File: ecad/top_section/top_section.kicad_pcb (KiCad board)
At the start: 4 copper layers, 100 x 88 mm, 142 parts, among them J1 JST PH, J2 JST PH, J3 JST SH, J4 JST SH, Q1 RE1C002UN, Q10 RE1C002UN, Q2 RE1C002UN, Q3 RE1C002UN, Q4 RE1C002UN, Q5 RE1C002UN, Q6 RE1C002UN, Q7 RE1C002UN, Q8 RE1C002UN, Q9 RE1C002UN, SW1 PEL12T, SW10 PEL12T, SW11 PEL12T, SW12 PEL12T, SW13 PEL12T, SW14 PEL12T, SW15 PEL12T, SW16 SW_Push, SW17 SW_Push, SW18 SW_Push, SW19 SW_Push, SW2 SW_Push, SW20 SW_Push, SW3 PEL12T, SW4 SW_Push, SW5 PEL12T, SW6 SW_Push, SW7 SW_Push, SW8 PEL12T, SW9 SW_Push, U11 ATtiny1617-M, U12 WS2811, U13 WS2811, U14 WS2811, U15 WS2811, U16 WS2811, U17 WS2811, U18 WS2811, U19 WS2811, U20 WS2811, U21 WS2811

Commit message: [WIP] Layouting a matric led driver
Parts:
- removed the C1 at (61.7, 60.8)
- removed C10, C11, C12, C13, C14, C15, C16, C17, C18, C19, C20, C4, C5, C6, C7, C8, C9: 100n, Capacitor_SMD:C_0603_1608Metric
- removed C22: 10u, Capacitor_SMD:C_0603_1608Metric
- removed Q1, Q10, Q2, Q3, Q4, Q5, Q6, Q7, Q8, Q9: RE1C002UN, Package_TO_SOT_SMD:SOT-416
- removed R1, R11, R13, R15, R17, R19, R21, R22, R23, R24, R25, R26, R3, R32, R33, R34, R35, R5, R7, R9: 68, Resistor_SMD:R_0603_1608Metric
- removed R10, R12, R14, R16, R18, R2, R20, R4, R6, R8: 11k, Resistor_SMD:R_0603_1608Metric
- removed R27, R29: 33, Resistor_SMD:R_0603_1608Metric
- removed U12, U13, U14, U15, U16, U17, U18, U19, U20, U21: WS2811, Package_SO:SOIC-8_3.9x4.9mm_P1.27mm
- added U2: LP5864, woodpecker:Texas_LP586X_VQFN-32-1EP_4x4mm_P0.4mm_EP2.8x2.8mm_ThermalVias, B.Cu at (107.0, 133.9)
- C2, C3: value 100n -> 1u; moved to F.Cu
- D10: value IN-PI32TAR -> 1N4148W; footprint woodpecker:LED_Inolux_IN-PI32TAR_PLCC4_3.2x2.8mm_P1.5mm -> Diode_SMD:D_SOD-123
- D11, D9: value 1N4148W -> LED_BGRA; footprint Diode_SMD:D_SOD-123 -> woodpecker:LED_Inolux_IN-PI32TRRRGB_PLCC4_3.2x2.8mm_P1.5mm
- D12, D16, D18, D20: value BAS16TW -> 1N4148W; footprint Package_TO_SOT_SMD:SOT-363_SC-70-6 -> Diode_SMD:D_SOD-123
- D13, D2, D21, D23, D25: value IN-PI32TAR -> LED_BGRA; footprint woodpecker:LED_Inolux_IN-PI32TAR_PLCC4_3.2x2.8mm_P1.5mm -> woodpecker:LED_Inolux_IN-PI32TRRRGB_PLCC4_3.2x2.8mm_P1.5mm
- D15, D17, D19: value BAS16TW -> LED_BGRA; footprint Package_TO_SOT_SMD:SOT-363_SC-70-6 -> woodpecker:LED_Inolux_IN-PI32TRRRGB_PLCC4_3.2x2.8mm_P1.5mm
- D27, D29, D5, D8: value IN-PI32TAR -> BAS16TW; footprint woodpecker:LED_Inolux_IN-PI32TAR_PLCC4_3.2x2.8mm_P1.5mm -> Package_TO_SOT_SMD:SOT-363_SC-70-6
- D28, D30, D6: value 1N4148W -> BAS16TW; footprint Diode_SMD:D_SOD-123 -> Package_TO_SOT_SMD:SOT-363_SC-70-6
- SW10, SW11, SW12, SW13, SW14, SW15, SW8: value PEL12T -> SW_Push; footprint woodpecker:PEL12T-4xxxS-S1024 -> woodpecker:SW_Hotswap_Kailh_MX_1.00u
- SW17, SW18, SW19, SW20, SW4, SW6, SW7: value SW_Push -> PEL12T; footprint woodpecker:SW_Hotswap_Kailh_MX_1.00u -> woodpecker:PEL12T-4xxxS-S1024
- moved C2 100.4 mm to (100.9, -7.45), turned to 0 degrees
- moved D16 86.7 mm to (142.2, 73.6)
- moved SW11 78.3 mm to (138.0, 82.0), turned to 0 degrees
- moved SW16 76.0 mm to (138.0, 120.0)
- moved C3 68.8 mm to (100.9, -4.93)
- moved SW7 60.1 mm to (62.0, 101.0), turned to -90 degrees
- moved D20 51.8 mm to (85.2, 111.6)
- moved D27 49.6 mm to (76.8, 99.5), turned to 90 degrees
- moved D19 46.2 mm to (81.0, 125.8), turned to 180 degrees
- moved D8 43.9 mm to (57.8, 99.5), turned to 90 degrees
- moved SW6 42.5 mm to (138.0, 63.0), turned to -90 degrees
- moved SW8 42.5 mm to (81.0, 82.0), turned to 0 degrees
- moved J1 41.4 mm to (141.4, 175.3)
- moved J3 40.0 mm to (122.4, 174.0)
- moved D7 38.0 mm to (133.8, 61.5), turned to 90 degrees
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- renumbered C21 to C1, J4 to J2, J2 to J3, J3 to J4, U11 to U1
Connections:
- C2 pad 1: +5V -> +3V3
- C3 pad 1: /RotaryEncoder_COL2/+5V_smooth -> +5V
- D1 pad 1: /COL1 -> (no net)
- D1 pad 6: /RotaryEncoder_COL1/Q_HS -> (no net)
- D10 pad 1: +5V -> /R2_SW
- D10 pad 2: /KeyboardKey_COL4/DOUT -> /KeyboardKey_COL2/SW_ND
- D11 pad 1: /R2_SW -> /C3_LEDB
- D11 pad 2: /KeyboardKey_COL4/SW_ND -> /C3_LEDG
- D12 pad 1: /COL4 -> /R2_SW
- D12 pad 2: /RotaryEncoder_COL4/H_QB -> /KeyboardKey_COL3/SW_ND
- D13 pad 1: +5V -> /C4_LEDB
- D13 pad 2: /KeyboardKey_COL5/DOUT -> /C4_LEDG
- D13 pad 3: GND -> /C4_LEDR
- D13 pad 4: /KeyboardKey_COL4/DOUT -> /R2_LEDA
- D14 pad 2: /KeyboardKey_COL5/SW_ND -> /KeyboardKey_COL4/SW_ND
- D15 pad 1: /COL5 -> /C5_LEDB
- D15 pad 2: /RotaryEncoder_COL5/H_QB -> /C5_LEDG
- D15 pad 3: /RotaryEncoder_COL5/H_QA -> /C5_LEDR
- D15 pad 4: /R1_QA -> /R2_LEDA
- D16 pad 1: /COL1 -> /R2_SW
- D16 pad 2: /RotaryEncoder_COL6/H_QB -> /KeyboardKey_COL5/SW_ND
- D17 pad 1: /COL2 -> /C1_LEDB
- D17 pad 2: /RotaryEncoder_COL7/H_QB -> /C1_LEDG
- D17 pad 3: /RotaryEncoder_COL7/H_QA -> /C1_LEDR
- D17 pad 4: /R3_QA -> /R4_LEDA
- D18 pad 1: /COL3 -> /R4_SW
- D18 pad 2: /RotaryEncoder_COL8/H_QB -> /KeyboardKey_COL6/SW_ND
- D19 pad 1: /COL4 -> /C2_LEDB
- D19 pad 2: /RotaryEncoder_COL9/H_QB -> /C2_LEDG
- D19 pad 3: /RotaryEncoder_COL9/H_QA -> /C2_LEDR
- D19 pad 4: /R3_QA -> /R4_LEDA
- D2 pad 1: +5V -> /C1_LEDB
- D2 pad 2: /KeyboardKey_COL1/DOUT -> /C1_LEDG
- D2 pad 3: GND -> /C1_LEDR
- D2 pad 4: /KeyboardKey_COL1/DIN -> /R2_LEDA
- D20 pad 1: /COL5 -> /R4_SW
- D20 pad 2: /RotaryEncoder_COL10/H_QB -> /KeyboardKey_COL7/SW_ND
- D21 pad 1: +5V -> /C3_LEDB
- D21 pad 2: /KeyboardKey_COL6/DOUT -> /C3_LEDG
- D21 pad 3: GND -> /C3_LEDR
- D21 pad 4: /KeyboardKey_COL6/DIN -> /R4_LEDA
- D22 pad 2: /KeyboardKey_COL6/SW_ND -> /KeyboardKey_COL8/SW_ND
- D23 pad 1: +5V -> /C4_LEDB
- D23 pad 2: /KeyboardKey_COL7/DOUT -> /C4_LEDG
- D23 pad 3: GND -> /C4_LEDR
- D23 pad 4: /KeyboardKey_COL6/DOUT -> /R4_LEDA
- D24 pad 2: /KeyboardKey_COL7/SW_ND -> /KeyboardKey_COL9/SW_ND
- D25 pad 1: +5V -> /C5_LEDB
- D25 pad 2: /KeyboardKey_COL8/DOUT -> /C5_LEDG
- D25 pad 3: GND -> /C5_LEDR
- D25 pad 4: /KeyboardKey_COL7/DOUT -> /R4_LEDA
- D26 pad 2: /KeyboardKey_COL8/SW_ND -> /KeyboardKey_COL10/SW_ND
- D27 pad 1: +5V -> (no net)
- D27 pad 2: /KeyboardKey_COL10/DIN -> /RotaryEncoder_COL7/H_QB
- D27 pad 3: GND -> /RotaryEncoder_COL7/H_QA
- D27 pad 4: /KeyboardKey_COL8/DOUT -> /R3_QA
- D28 pad 1: /R4_SW -> (no net)
- D28 pad 2: /KeyboardKey_COL9/SW_ND -> /RotaryEncoder_COL8/H_QB
- D29 pad 1: +5V -> (no net)
- D29 pad 2: /KeyboardKey_COL10/DOUT -> /RotaryEncoder_COL9/H_QB
- D29 pad 3: GND -> /RotaryEncoder_COL9/H_QA
- D29 pad 4: /KeyboardKey_COL10/DIN -> /R3_QA
- D30 pad 1: /R4_SW -> (no net)
- D30 pad 2: /KeyboardKey_COL10/SW_ND -> /RotaryEncoder_COL10/H_QB
- D4 pad 1: /COL2 -> (no net)
- D4 pad 6: /RotaryEncoder_COL2/Q_HS -> (no net)
- D5 pad 1: +5V -> (no net)
- D5 pad 2: /KeyboardKey_COL2/DOUT -> /RotaryEncoder_COL3/H_QB
- D5 pad 3: GND -> /RotaryEncoder_COL3/H_QA
- D5 pad 4: /KeyboardKey_COL1/DOUT -> /R1_QA
- D6 pad 1: /R2_SW -> (no net)
- D6 pad 2: /KeyboardKey_COL2/SW_ND -> /RotaryEncoder_COL4/H_QB
- D7 pad 1: /COL3 -> (no net)
- D7 pad 2: /RotaryEncoder_COL3/H_QB -> /RotaryEncoder_COL5/H_QB
- D7 pad 3: /RotaryEncoder_COL3/H_QA -> /RotaryEncoder_COL5/H_QA
- D7 pad 6: /RotaryEncoder_COL3/Q_HS -> (no net)
- D8 pad 1: +5V -> (no net)
- D8 pad 2: /KeyboardKey_COL3/DOUT -> /RotaryEncoder_COL6/H_QB
- D8 pad 3: GND -> /RotaryEncoder_COL6/H_QA
- D8 pad 4: /KeyboardKey_COL2/DOUT -> /R3_QA
- D9 pad 1: /R2_SW -> /C2_LEDB
- D9 pad 2: /KeyboardKey_COL3/SW_ND -> /C2_LEDG
- SW1 pad 1: /RotaryEncoder_COL1/OUTR -> /C1_LEDR
- SW1 pad 2: /RotaryEncoder_COL1/OUTG -> /C1_LEDG
- SW1 pad 3: /RotaryEncoder_COL1/H_SW -> unconnected-(SW1-Pad3)
- SW1 pad 4: /RotaryEncoder_COL1/OUTB -> /C1_LEDB
- SW1 pad 5: +5V -> /R1_LEDA
- SW10 pad 1: /RotaryEncoder_COL5/OUTR -> /COL4
- SW10 pad 2: /RotaryEncoder_COL5/OUTG -> /KeyboardKey_COL4/SW_ND
- SW11 pad 1: /RotaryEncoder_COL6/OUTR -> /COL5
- SW11 pad 2: /RotaryEncoder_COL6/OUTG -> /KeyboardKey_COL5/SW_ND
- SW12 pad 1: /RotaryEncoder_COL7/OUTR -> /COL1
- SW12 pad 2: /RotaryEncoder_COL7/OUTG -> /KeyboardKey_COL6/SW_ND
- SW13 pad 1: /RotaryEncoder_COL8/OUTR -> /COl2
- SW13 pad 2: /RotaryEncoder_COL8/OUTG -> /KeyboardKey_COL7/SW_ND
- SW14 pad 1: /RotaryEncoder_COL9/OUTR -> /COL3
- SW14 pad 2: /RotaryEncoder_COL9/OUTG -> /KeyboardKey_COL8/SW_ND
- SW15 pad 1: /RotaryEncoder_COL10/OUTR -> /COL4
- SW15 pad 2: /RotaryEncoder_COL10/OUTG -> /KeyboardKey_COL9/SW_ND
- SW16 pad 1: /COL1 -> /COL5
- SW16 pad 2: /KeyboardKey_COL6/SW_ND -> /KeyboardKey_COL10/SW_ND
- SW17 pad 1: /COL2 -> /C2_LEDR
- SW17 pad 2: /KeyboardKey_COL7/SW_ND -> /C2_LEDG
- SW18 pad 1: /COL3 -> /C3_LEDR
- SW18 pad 2: /KeyboardKey_COL8/SW_ND -> /C3_LEDG
- SW19 pad 1: /COL4 -> /C4_LEDR
- SW19 pad 2: /KeyboardKey_COL9/SW_ND -> /C4_LEDG
- SW20 pad 1: /COL5 -> /C5_LEDR
- SW20 pad 2: /KeyboardKey_COL10/SW_ND -> /C5_LEDG
- SW3 pad 1: /RotaryEncoder_COL2/OUTR -> /C2_LEDR
- SW3 pad 2: /RotaryEncoder_COL2/OUTG -> /C2_LEDG
- SW3 pad 3: /RotaryEncoder_COL2/H_SW -> unconnected-(SW3-Pad3)
- SW3 pad 4: /RotaryEncoder_COL2/OUTB -> /C2_LEDB
- SW3 pad 5: +5V -> /R1_LEDA
- SW3 pad C: /COL2 -> /COl2
- SW4 pad 1: /COL2 -> /C3_LEDR
- SW4 pad 2: /KeyboardKey_COL2/SW_ND -> /C3_LEDG
- SW5 pad 1: /RotaryEncoder_COL3/OUTR -> /C4_LEDR
- SW5 pad 2: /RotaryEncoder_COL3/OUTG -> /C4_LEDG
- SW5 pad 3: /RotaryEncoder_COL3/H_SW -> unconnected-(SW5-Pad3)
- SW5 pad 4: /RotaryEncoder_COL3/OUTB -> /C4_LEDB
- SW5 pad 5: +5V -> /R1_LEDA
- SW5 pad A: /RotaryEncoder_COL3/H_QA -> /RotaryEncoder_COL4/H_QA
- SW5 pad B: /RotaryEncoder_COL3/H_QB -> /RotaryEncoder_COL4/H_QB
- SW5 pad C: /COL3 -> /COL4
- SW6 pad 1: /COL3 -> /C5_LEDR
- SW6 pad 2: /KeyboardKey_COL3/SW_ND -> /C5_LEDG
- SW7 pad 1: /COL4 -> /C1_LEDR
- SW7 pad 2: /KeyboardKey_COL4/SW_ND -> /C1_LEDG
- SW8 pad 1: /RotaryEncoder_COL4/OUTR -> /COl2
- SW8 pad 2: /RotaryEncoder_COL4/OUTG -> /KeyboardKey_COL2/SW_ND
- SW9 pad 1: /COL5 -> /COL3
- SW9 pad 2: /KeyboardKey_COL5/SW_ND -> /KeyboardKey_COL3/SW_ND
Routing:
- net +5V: track 478.9 -> 0.00 mm, vias 10 -> 0
- net /R1_SW: track 186.5 -> 0.00 mm
- net GND: track 161.1 -> 0.00 mm, vias 55 -> 0
- net /R4_LEDA: track 0.00 -> 159.5 mm, vias 0 -> 5
- net /R2_LEDA: track 0.00 -> 159.5 mm, vias 0 -> 5
- net /R3_SW: track 152.1 -> 0.00 mm, vias 2 -> 0
- net /R3_QA: track 142.4 -> 4.35 mm, vias 2 -> 5
- net /R3_QB: track 139.8 -> 7.25 mm, vias 2 -> 5
- net /R4_SW: track 114.8 -> 6.75 mm, vias 0 -> 5
- net /COL5: track 153.7 -> 46.3 mm, vias 3 -> 0
- net /R1_LEDA: track 0.00 -> 100.4 mm
- net /COL2: track 98.2 -> 0.00 mm, vias 3 -> 0
- net /R1_QA: track 181.1 -> 87.8 mm, vias 0 -> 5
- net /C2_LEDB: track 0.00 -> 88.5 mm
- net /C4_LEDB: track 0.00 -> 88.5 mm
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- removed copper zone on In1.Cu, net GND
- removed copper zone on In2.Cu, net GND

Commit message: [WIP] Layouting a matric led driver
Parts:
- added C4: 1n, Capacitor_SMD:C_0402_1005Metric, B.Cu at (105.0, 137.3)
- added C5: 1u, Capacitor_SMD:C_0402_1005Metric, B.Cu at (108.4, 137.3)
- C2, C3: footprint Capacitor_SMD:C_0603_1608Metric -> Capacitor_SMD:C_0402_1005Metric; moved to B.Cu
- moved C2 144.3 mm to (103.6, 136.8), turned to -90 degrees
- moved C3 136.3 mm to (108.8, 131.1)
- moved U2 0.30 mm to (107.1, 134.2)
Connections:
- U2 pad 25: unconnected-(U2-VCAP-Pad25) -> Net-(U2-VCAP)
- U2 pad 26: unconnected-(U2-IF-Pad26) -> GND
- U2 pad 27: unconnected-(U2-VSYNC-Pad27) -> GND
- U2 pad 32: unconnected-(U2-VIO_EN-Pad32) -> Net-(U2-VIO_EN)
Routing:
- net /C5_LEDR: track 84.6 -> 128.2 mm
- net /C5_LEDB: track 68.8 -> 88.3 mm
- net /R4_LEDA: track 159.5 -> 140.6 mm
- net unconnected-(U2-ADDR0/MISO-Pad30): track 0.00 -> 5.04 mm
- net unconnected-(U2-ADDR1/SS-Pad31): track 0.00 -> 4.42 mm
- net /C3_LEDB: track 86.0 -> 89.1 mm
- net /C1_LEDB: track 72.0 -> 74.7 mm
- net /C1_LEDG: track 63.9 -> 66.0 mm
- added copper zone on In1.Cu, net GND
- added copper zone on In2.Cu, net GND

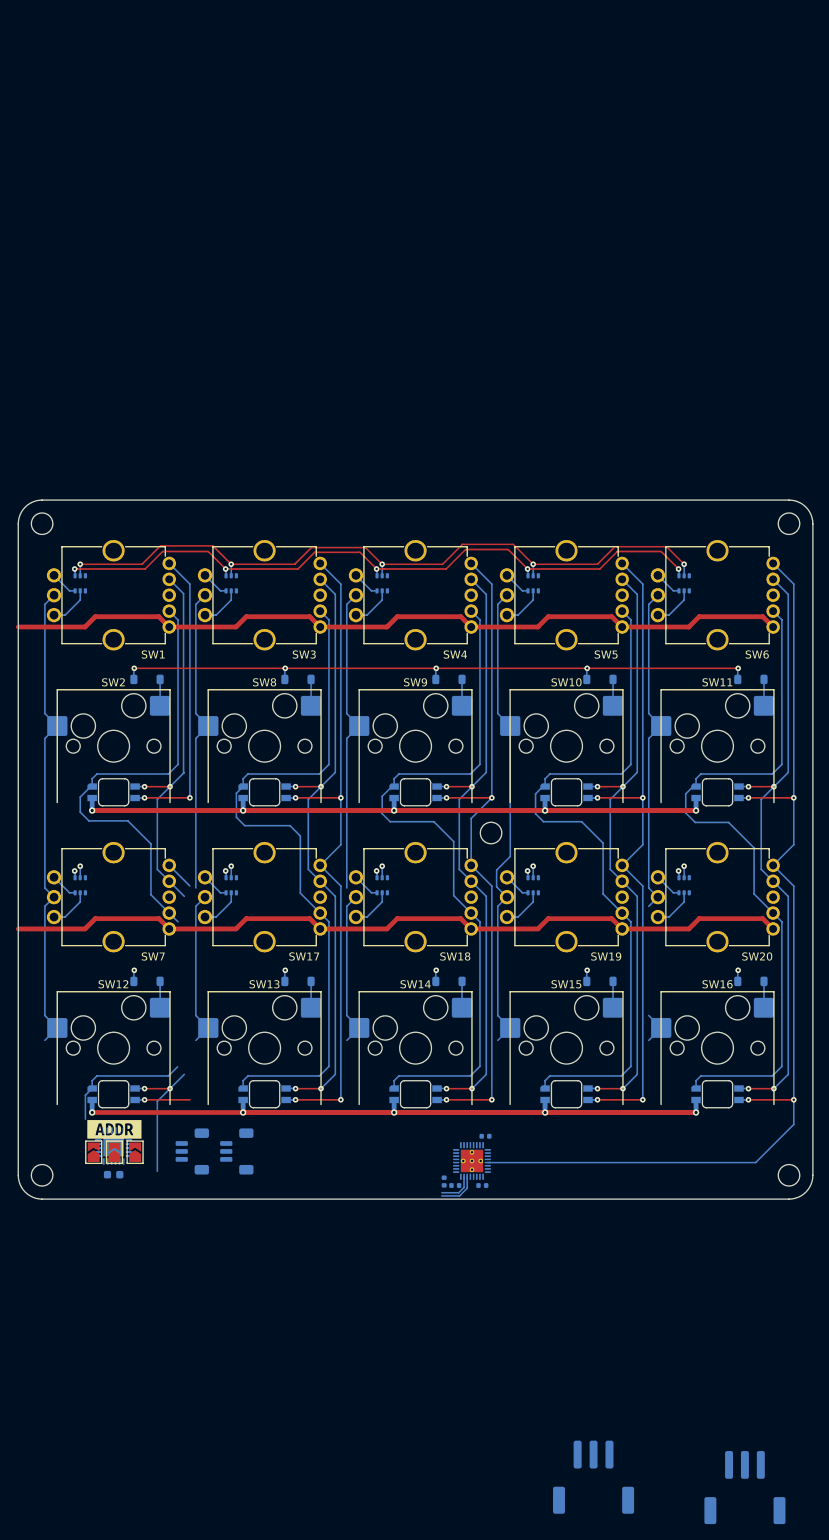
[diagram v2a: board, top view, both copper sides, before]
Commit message: Uses a LP5864 LED Matrix Driver for Top Section
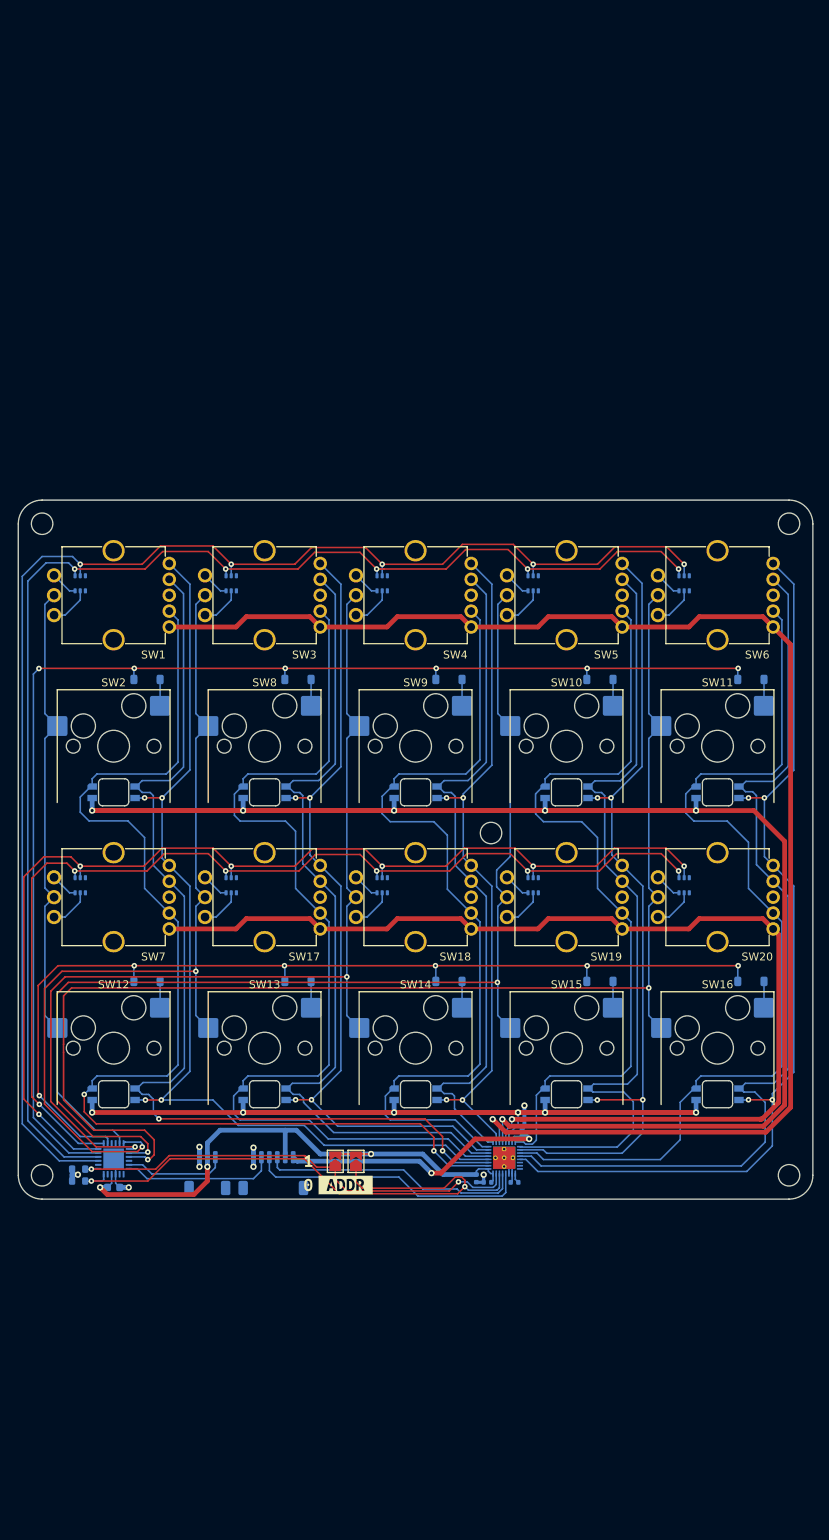
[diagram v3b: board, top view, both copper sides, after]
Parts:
- removed J3: JST PH, woodpecker:JST_PH_S3B-PH-SM4-TB_1x03-1MP_P2.00mm_Horizontal
- removed J4: JST SH, woodpecker:JST_SH_BM03B-SRSS-TB_1x03-1MP_P1.00mm_Vertical
- removed JP3: SolderJumper_2_Open, Jumper:SolderJumper-2_P1.3mm_Open_TrianglePad1.0x1.5mm
- removed kibuzzard-68C2D93D: G***, kibuzzard-68C2D93D
- removed kibuzzard-68C2D94D: G***, kibuzzard-68C2D94D
- removed kibuzzard-68C2D9C3: G***, kibuzzard-68C2D9C3
- added R1: 10k, Resistor_SMD:R_0603_1608Metric, B.Cu at (57.6, 136.7)
- added R2: 10k, Resistor_SMD:R_0603_1608Metric, B.Cu at (57.6, 135.2)
- added kibuzzard-68CBF0CC: G***, kibuzzard-68CBF0CC, F.Cu at (86.5, 135.7)
- added kibuzzard-68CBF276: G***, kibuzzard-68CBF276, B.Cu at (83.6, 130.8)
- J1: value JST PH -> Conn_01x06; footprint woodpecker:JST_PH_S3B-PH-SM4-TB_1x03-1MP_P2.00mm_Horizontal -> Connector_JST:JST_SH_SM06B-SRSS-TB_1x06-1MP_P1.00mm_Horizontal
- J2: footprint woodpecker:JST_SH_BM03B-SRSS-TB_1x03-1MP_P1.00mm_Vertical -> woodpecker:JST_SH_SM03B-SRSS-TB_1x03-1MP_P1.00mm_Horizontal
- moved J1 71.3 mm to (82.1, 135.7)
- moved kibuzzard-68B5BEB6 29.9 mm to (91.2, 137.2)
- moved JP2 27.8 mm to (89.9, 134.2)
- moved JP1 27.8 mm to (92.5, 134.2)
- moved kibuzzard-68C2D999 7.89 mm to (73.8, 130.8)
- moved C3 4.62 mm to (113.4, 130.6), turned to 90 degrees
- moved J2 4.60 mm to (73.8, 135.7), turned to 180 degrees
- moved C2 4.07 mm to (107.7, 136.4)
- moved U2 4.07 mm to (111.2, 133.8)
- moved C4 4.07 mm to (109.0, 136.9)
- moved C5 4.07 mm to (112.5, 136.9)
- moved U1 1.61 mm to (62.0, 133.9)
- moved C1 1.61 mm to (62.0, 137.5)
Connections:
- C4 pad 1: Net-(U2-VIO_EN) -> +3V3
- J1 pad 2: /DIN -> +3V3
- J1 pad 3: GND -> /SDA
- JP1 pad 2: GND -> +3V3
- JP2 pad 2: GND -> +3V3
- SW13 pad 1: /COl2 -> /COL2
- SW17 pad C: /COl2 -> /COL2
- SW18 pad 5: /RotaryEncoder_COL8/LEDA -> /R3_LEDA
- SW19 pad 5: /RotaryEncoder_COL9/LEDA -> /R3_LEDA
- SW3 pad C: /COl2 -> /COL2
- SW8 pad 1: /COl2 -> /COL2
- U1 pad 10: /R1_QB -> /R1_QA
- U1 pad 11: /R1_SW -> /R2_SW
- U1 pad 12: /R2_SW -> /R3_QB
- U1 pad 13: /R4_SW -> /R3_QA
- U1 pad 14: /R3_QA -> /R4_SW
- U1 pad 15: /R3_QB -> unconnected-(U1-PB1-Pad15)
- U1 pad 16: /R3_SW -> unconnected-(U1-PB0-Pad16)
- U1 pad 8: /A2 -> unconnected-(U1-PA7-Pad8)
- U1 pad 9: /R1_QA -> /R1_QB
- U2 pad 28: unconnected-(U2-SCL/SCLK-Pad28) -> /SCL
- U2 pad 29: unconnected-(U2-SDA/MOSI-Pad29) -> /SDA
- U2 pad 30: unconnected-(U2-ADDR0/MISO-Pad30) -> /A0
- U2 pad 31: unconnected-(U2-ADDR1/SS-Pad31) -> /A1
- U2 pad 32: Net-(U2-VIO_EN) -> +3V3
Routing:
- net /R3_QB: track 7.25 -> 139.3 mm, vias 5 -> 6
- net /R3_QA: track 4.35 -> 133.1 mm, vias 5 -> 6
- net /R4_SW: track 6.75 -> 124.5 mm, vias 5 -> 6
- net /COL5: track 46.3 -> 163.9 mm, vias 0 -> 2
- net /COL2: track 0.00 -> 110.2 mm, vias 0 -> 2
- net /R1_QB: track 90.8 -> 179.9 mm
- net /R1_QA: track 87.8 -> 173.6 mm
- net /R2_LEDA: track 159.5 -> 245.3 mm, vias 5 -> 6
- net /COL4: track 60.2 -> 144.6 mm, vias 0 -> 2
- net /R1_LEDA: track 100.4 -> 184.4 mm, vias 0 -> 1
- net /R3_LEDA: track 60.2 -> 140.1 mm, vias 0 -> 1
- net /R2_SW: track 83.1 -> 161.9 mm, vias 5 -> 6
- net /A0: track 0.00 -> 77.3 mm, vias 0 -> 2
- net /C1_LEDR: track 48.1 -> 124.0 mm, vias 3 -> 4
- net /C1_LEDB: track 74.7 -> 146.6 mm, vias 0 -> 2
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
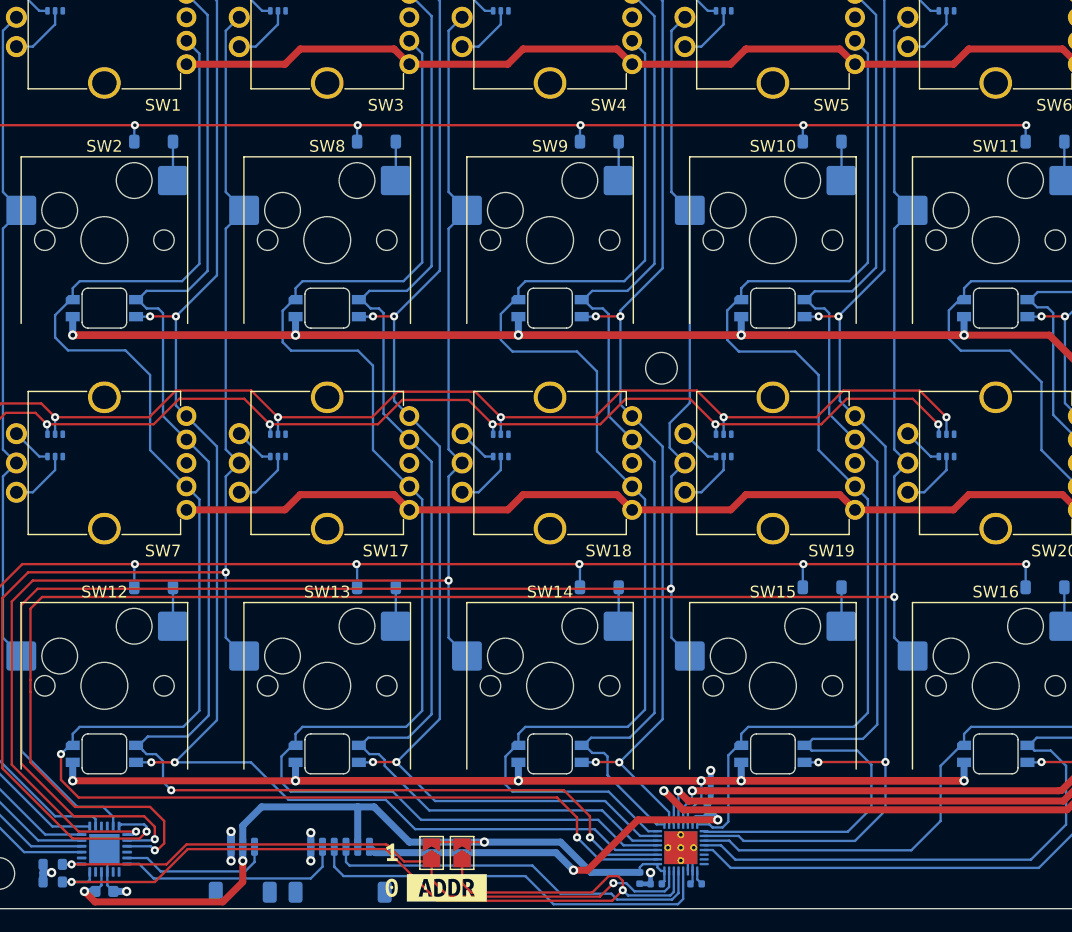
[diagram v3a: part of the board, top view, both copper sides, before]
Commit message: Uses LED Matrix controller on all board.
It simplifies so much the design for a small cost.
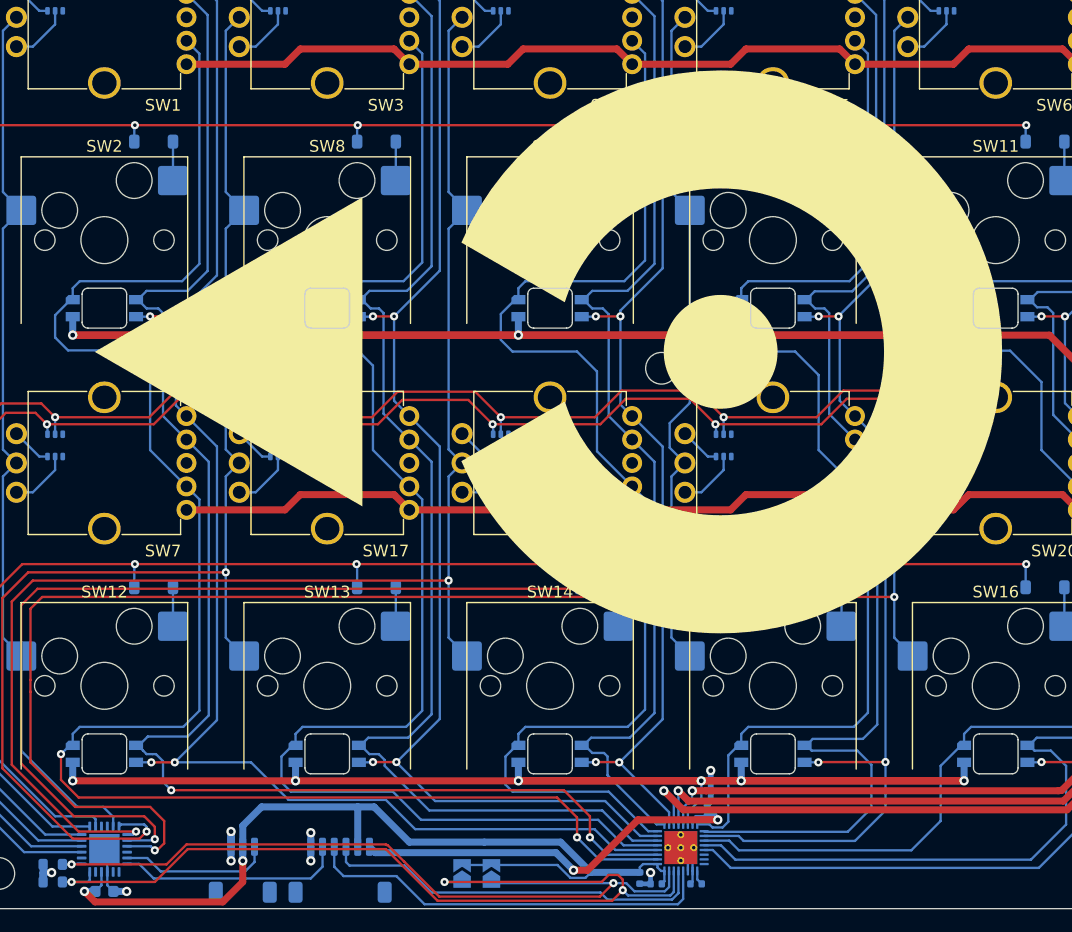
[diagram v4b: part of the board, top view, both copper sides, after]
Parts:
- removed kibuzzard-68B5BEB6: G***, kibuzzard-68B5BEB6
- removed kibuzzard-68CBF0CC: G***, kibuzzard-68CBF0CC
- added kibuzzard-68CC2B7E: G***, kibuzzard-68CC2B7E, B.Cu at (93.8, 133.5)
- added kibuzzard-68CC2B91: G***, kibuzzard-68CC2B91, B.Cu at (98.6, 136.0)
- JP1, JP2: moved to B.Cu
- moved JP2 5.39 mm to (95.0, 136.0)
- moved JP1 1.75 mm to (92.5, 136.0)
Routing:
- net /R4_LEDA: track 144.8 -> 125.8 mm
- net /A1: track 58.3 -> 67.9 mm
- net +3V3: track 71.4 -> 78.3 mm, vias 3 -> 2
- net /A0: track 77.3 -> 77.9 mm, vias 2 -> 3
